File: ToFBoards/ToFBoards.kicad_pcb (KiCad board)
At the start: 2 copper layers, 1 part, among them U1 VL53L1X

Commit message: ToF boards
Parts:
- added C1: 100n, Capacitors_SMD:C_0402, F.Cu at (151.2, 105.0)
- added C2: 4.7u, Capacitors_SMD:C_0402, F.Cu at (151.2, 103.3)
- added J1: Bottom, ToFTop, B.Cu at (148.6, 103.3)
- added J2: Top, ToFBottom, B.Cu at (148.6, 105.1)
- moved U1 0.12 mm to (148.6, 104.9), turned to 90 degrees
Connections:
- U1 pad 1: Net-(U1-Pad1) -> VCC
- U1 pad 10: (no net) -> SCL
- U1 pad 11: (no net) -> VCC
- U1 pad 12: (no net) -> GND
- U1 pad 2: (no net) -> GND
- U1 pad 3: (no net) -> GND
- U1 pad 4: (no net) -> GND
- U1 pad 5: (no net) -> SIGNAL
- U1 pad 6: (no net) -> GND
- U1 pad 9: (no net) -> SDA
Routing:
- net GND: track 0.00 -> 12.6 mm, vias 0 -> 1
- net VCC: track 0.00 -> 12.1 mm, vias 0 -> 2
- net SDA: track 0.00 -> 7.22 mm, vias 0 -> 1
- net SIGNAL: track 0.00 -> 6.44 mm, vias 0 -> 1
- net SCL: track 0.00 -> 3.55 mm, vias 0 -> 1
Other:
- board outline added: 8.7 x 4.9 mm

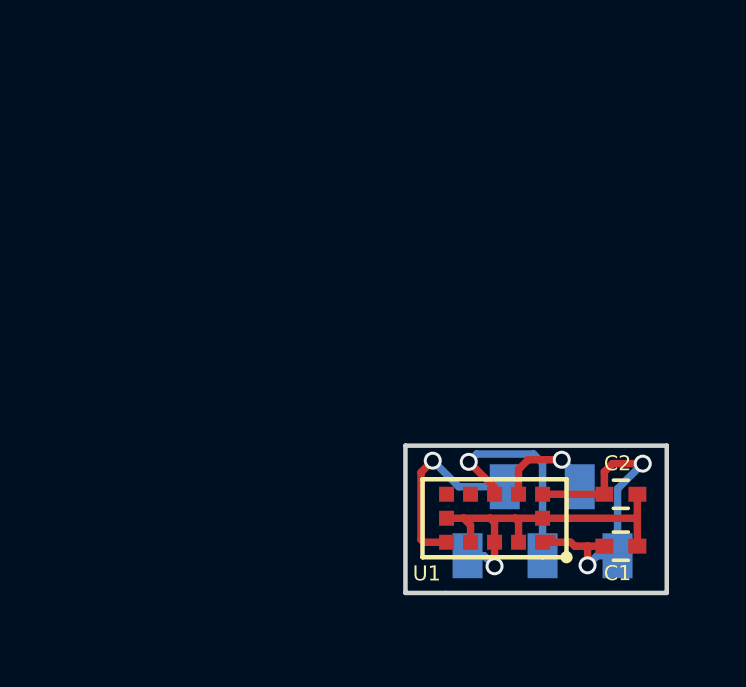
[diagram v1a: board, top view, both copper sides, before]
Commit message: complete ToF boards
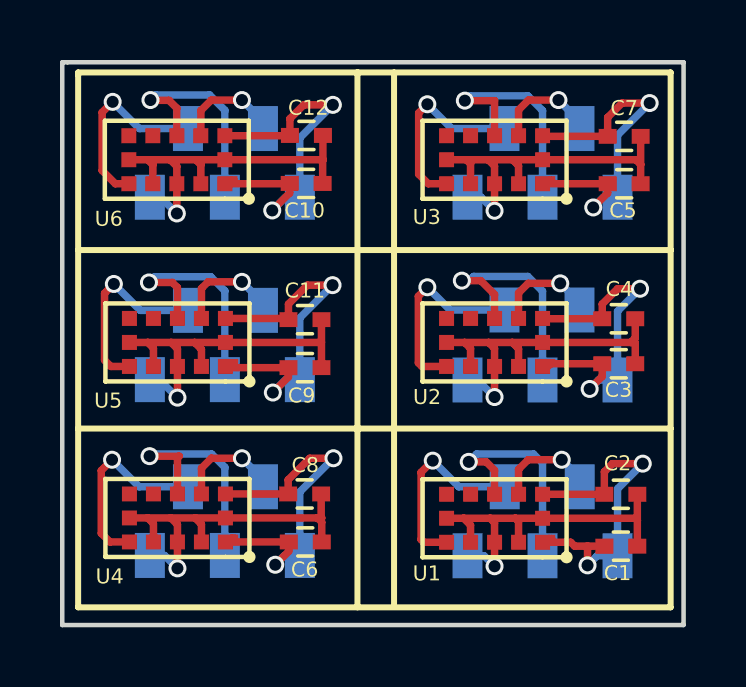
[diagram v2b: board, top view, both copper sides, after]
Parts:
- added C10: 100n, Capacitors_SMD:C_0402, F.Cu at (140.7, 92.9)
- added C11: 4.7u, Capacitors_SMD:C_0402, F.Cu at (140.6, 97.5)
- added C12: 4.7u, Capacitors_SMD:C_0402, F.Cu at (140.7, 91.3)
- added C3: 100n, Capacitors_SMD:C_0402, F.Cu at (151.1, 99.0)
- added C4: 4.7u, Capacitors_SMD:C_0402, F.Cu at (151.1, 97.5)
- added C5: 100n, Capacitors_SMD:C_0402, F.Cu at (151.3, 93.0)
- added C6: 100n, Capacitors_SMD:C_0402, F.Cu at (140.7, 104.9)
- added C7: 4.7u, Capacitors_SMD:C_0402, F.Cu at (151.3, 91.4)
- added C8: 4.7u, Capacitors_SMD:C_0402, F.Cu at (140.6, 103.3)
- added C9: 100n, Capacitors_SMD:C_0402, F.Cu at (140.6, 99.1)
- added J10: Bot, footprint:ToFBottom, B.Cu at (138.0, 99.2)
- added J11: Top, footprint:ToFTop, B.Cu at (138.0, 91.4)
- added J12: Bot, footprint:ToFBottom, B.Cu at (138.0, 93.2)
- added J3: Top, footprint:ToFTop, B.Cu at (148.5, 97.4)
- added J4: Bot, footprint:ToFBottom, B.Cu at (148.6, 99.2)
- added J5: Top, footprint:ToFTop, B.Cu at (148.5, 91.4)
- added J6: Bot, footprint:ToFBottom, B.Cu at (148.6, 93.2)
- added J7: Top, footprint:ToFTop, B.Cu at (138.0, 103.3)
- added J8: Bot, footprint:ToFBottom, B.Cu at (138.0, 105.1)
- added J9: Top, footprint:ToFTop, B.Cu at (138.0, 97.4)
- added U2: VL53L1X, footprint:VL53L1X, F.Cu at (148.6, 99.0)
- added U3: VL53L1X, footprint:VL53L1X, F.Cu at (148.6, 93.0)
- added U4: VL53L1X, footprint:VL53L1X, F.Cu at (138.0, 104.9)
- added U5: VL53L1X, footprint:VL53L1X, F.Cu at (138.0, 99.0)
- added U6: VL53L1X, footprint:VL53L1X, F.Cu at (138.0, 93.0)
- J1: value Bottom -> Top; footprint ToFTop -> footprint:ToFTop
- J2: value Top -> Bot; footprint ToFBottom -> footprint:ToFBottom
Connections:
- net GND renamed GND1
- net SCL renamed SCL1
- net SDA renamed SDA1
- net SIGNAL renamed SIGNAL1
- net VCC renamed VCC1
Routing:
- net GND3: track 0.00 -> 12.9 mm, vias 0 -> 1
- net GND6: track 0.00 -> 12.8 mm, vias 0 -> 1
- net GND4: track 0.00 -> 12.7 mm, vias 0 -> 1
- net GND5: track 0.00 -> 12.7 mm, vias 0 -> 1
- net GND2: track 0.00 -> 12.7 mm, vias 0 -> 1
- net VCC6: track 0.00 -> 12.6 mm, vias 0 -> 2
- net VCC3: track 0.00 -> 12.6 mm, vias 0 -> 2
- net VCC4: track 0.00 -> 12.5 mm, vias 0 -> 2
- net VCC5: track 0.00 -> 12.4 mm, vias 0 -> 2
- net VCC2: track 0.00 -> 11.8 mm, vias 0 -> 2
- net SDA2: track 0.00 -> 7.99 mm, vias 0 -> 1
- net SDA5: track 0.00 -> 7.94 mm, vias 0 -> 1
- net SDA4: track 0.00 -> 7.91 mm, vias 0 -> 1
- net SDA3: track 0.00 -> 7.81 mm, vias 0 -> 1
- net SDA6: track 0.00 -> 7.57 mm, vias 0 -> 1
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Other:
- board size 8.7 x 4.9 mm -> 20.7 x 18.8 mm
